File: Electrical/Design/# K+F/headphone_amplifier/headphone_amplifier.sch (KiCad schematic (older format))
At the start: 6 parts

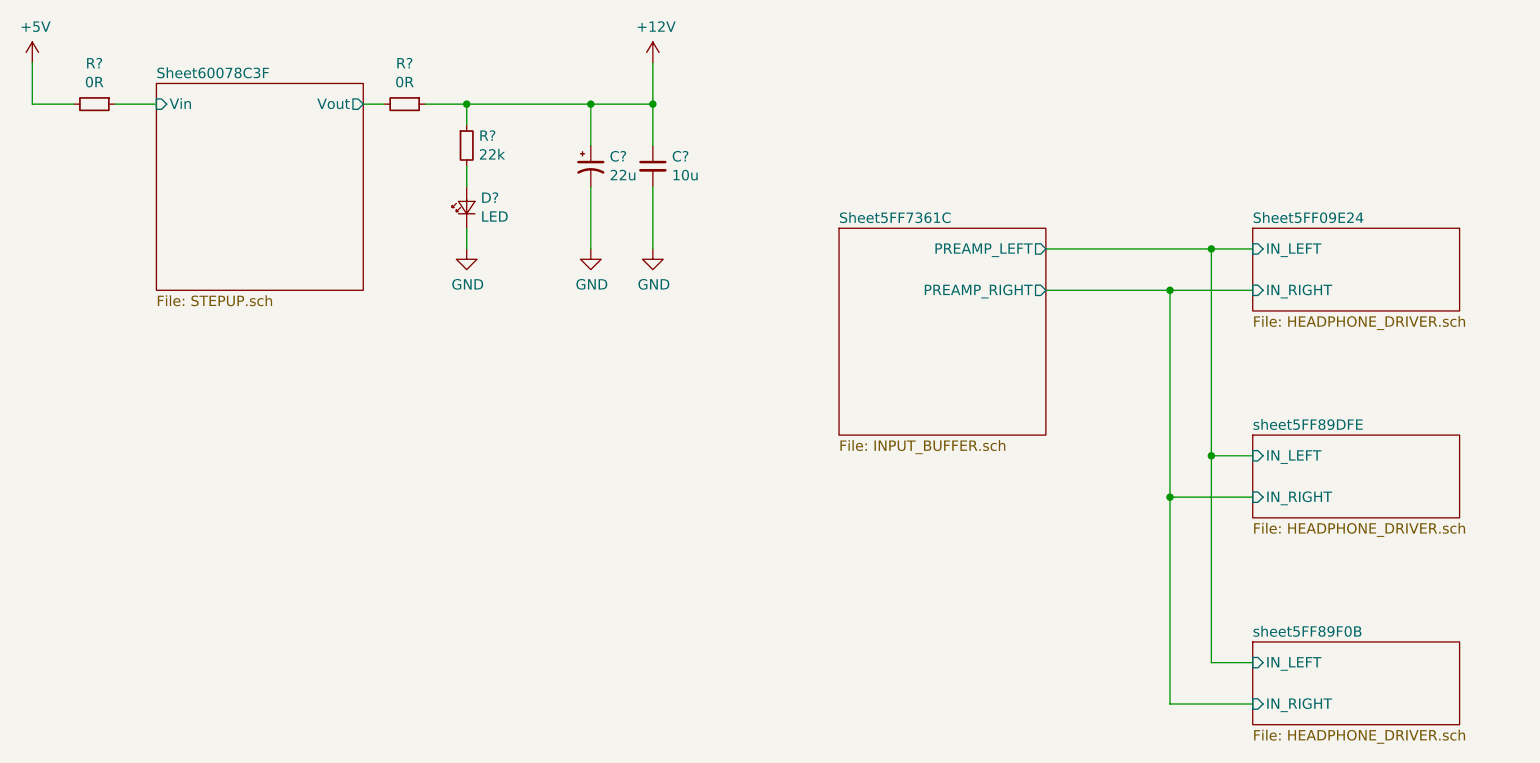
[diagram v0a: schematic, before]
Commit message: SUKU headphone_amplifier schematic fix and simulation added
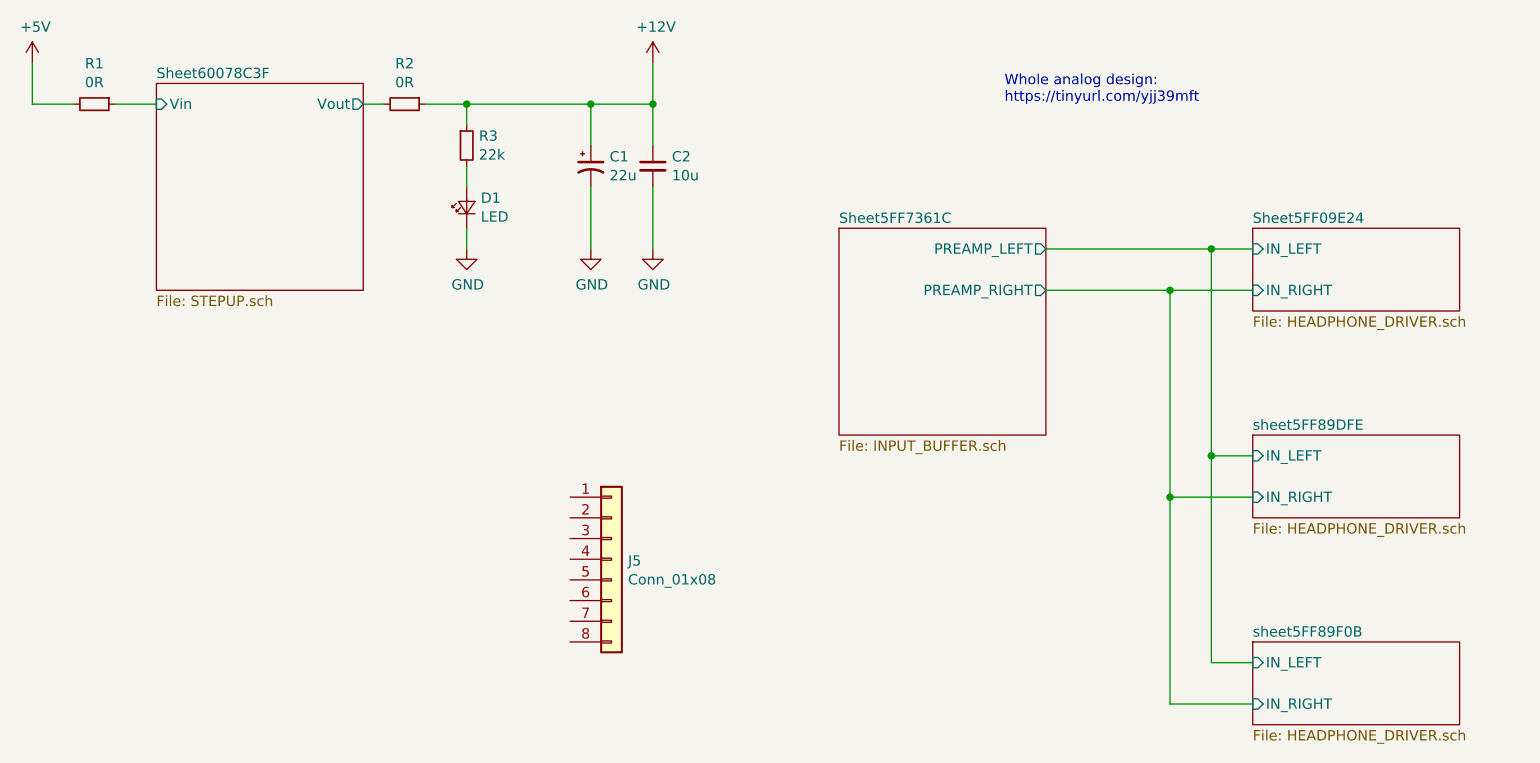
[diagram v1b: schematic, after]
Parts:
- added J5: Conn_01x08, suku_basics:grid_outline, symbol Connector_Generic:Conn_01x08
- gave numbers to parts that had none: 6
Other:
- note added: "Whole analog design:\nhttps://tinyurl.com/yjj39mft"
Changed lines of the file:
@@
 $EndDescr
 $Comp
-L suku_basics:LED D?
+L suku_basics:LED D1
 U 1 1 5FEE4BEA
 P 5700 2500
-F 0 "D?" V 5746 2432 50  0000 R CNN
+F 0 "D1" V 5746 2432 50  0000 R CNN
 F 1 "LED" V 5655 2432 50  0000 R CNN
 F 2 "suku_basics:LED_0805" V 5700 2500 50  0001 C CNN
@@
 $EndComp
 $Comp
-L power:+12V #PWR?
+L power:+12V #PWR04
 U 1 1 5FEE6012
 P 6600 1800
-F 0 "#PWR?" H 6600 1650 50  0001 C CNN
+F 0 "#PWR04" H 6600 1650 50  0001 C CNN
 F 1 "+12V" H 6615 1973 50  0000 C CNN
 F 2 "" H 6600 1800 50  0001 C CNN
@@
 $EndComp
 $Comp
-L suku_basics:RES R?
+L suku_basics:RES R3
 U 1 1 5FEE69AC
 P 5700 2200
-F 0 "R?" H 5759 2246 50  0000 L CNN
+F 0 "R3" H 5759 2246 50  0000 L CNN
 F 1 "22k" H 5759 2155 50  0000 L CNN
 F 2 "suku_basics:RES_0805" H 5700 2200 50  0001 C CNN
@@
 $EndComp
 $Comp
-L power:GND #PWR?
+L power:GND #PWR02
 U 1 1 5FEE7098
 P 5700 2700
-F 0 "#PWR?" H 5700 2450 50  0001 C CNN
+F 0 "#PWR02" H 5700 2450 50  0001 C CNN
 F 1 "GND" H 5705 2527 50  0000 C CNN
 F 2 "" H 5700 2700 50  0001 C CNN
@@
 	6600 2000 6600 1800
 $Comp
-L suku_basics:CAP C?
+L suku_basics:CAP C2
 U 1 1 5FF99EA8
 P 6600 2300
-F 0 "C?" H 6692 2346 50  0000 L CNN
+F 0 "C2" H 6692 2346 50  0000 L CNN
 F 1 "10u" H 6692 2255 50  0000 L CNN
 F 2 "suku_basics:CAP_0805" H 6600 2300 50  0001 C CNN
@@
 $EndComp
 $Comp
-L suku_basics:CAP_POL C?
+L suku_basics:CAP_POL C1
 U 1 1 5FF9BCBF
 P 6300 2300
-AR Path="/5FF9BCBF" Ref="C?"  Part="1"
+AR Path="/5FF9BCBF" Ref="C1"  Part="1"
 AR Path="/5FF7361D/5FF9BCBF" Ref="C?"  Part="1"
-F 0 "C?" H 6391 2346 50  0000 L CNN
+F 0 "C1" H 6391 2346 50  0000 L CNN
 F 1 "22u" H 6391 2255 50  0000 L CNN
 F 2 "" H 6300 2300 50  0001 C CNN
@@
 $EndComp
 $Comp
-L power:GND #PWR?
+L power:GND #PWR03
 U 1 1 5FF9CB04
 P 6300 2700
-F 0 "#PWR?" H 6300 2450 50  0001 C CNN
+F 0 "#PWR03" H 6300 2450 50  0001 C CNN
 F 1 "GND" H 6305 2527 50  0000 C CNN
 F 2 "" H 6300 2700 50  0001 C CNN
@@
 	6300 2700 6300 2400
 $Comp
-L power:GND #PWR?
+L power:GND #PWR05
 U 1 1 5FF9D16F
 P 6600 2700
-F 0 "#PWR?" H 6600 2450 50  0001 C CNN
+F 0 "#PWR05" H 6600 2450 50  0001 C CNN
 F 1 "GND" H 6605 2527 50  0000 C CNN
 F 2 "" H 6600 2700 50  0001 C CNN
@@
 Connection ~ 6600 2000
 $Comp
-L suku_basics:RES R?
+L suku_basics:RES R1
 U 1 1 60074023
 P 3900 2000
-F 0 "R?" V 3704 2000 50  0000 C CNN
+F 0 "R1" V 3704 2000 50  0000 C CNN
 F 1 "0R" V 3795 2000 50  0000 C CNN
 F 2 "suku_basics:RES_0805" H 3900 2000 50  0001 C CNN
@@
 	3800 2000 3600 2000
 $Comp
-L power:+5V #PWR?
+L power:+5V #PWR01
 U 1 1 6007402A
 P 3600 1800
-F 0 "#PWR?" H 3600 1650 50  0001 C CNN
+F 0 "#PWR01" H 3600 1650 50  0001 C CNN
 F 1 "+5V" H 3615 1973 50  0000 C CNN
 F 2 "" H 3600 1800 50  0001 C CNN
@@
 	3600 1800 3600 2000
 $Comp
-L suku_basics:RES R?
+L suku_basics:RES R2
 U 1 1 600765BD
 P 5400 2000
-F 0 "R?" V 5204 2000 50  0000 C CNN
+F 0 "R2" V 5204 2000 50  0000 C CNN
 F 1 "0R" V 5295 2000 50  0000 C CNN
 F 2 "suku_basics:RES_0805" H 5400 2000 50  0001 C CNN
@@
 Wire Wire Line
 	4000 2000 4200 2000
+Text Notes 8300 2000 0    50   ~ 0
+Whole analog design:\nhttps://tinyurl.com/yjj39mft
+$Comp
+L Connector_Generic:Conn_01x08 J5
+U 1 1 605AEAE2
+P 6400 4200
+F 0 "J5" H 6480 4192 50  0000 L CNN
+F 1 "Conn_01x08" H 6480 4101 50  0000 L CNN
+F 2 "suku_basics:grid_outline" H 6400 4200 50  0001 C CNN
+F 3 "~" H 6400 4200 50  0001 C CNN
+	1    6400 4200
+	1    0    0    -1
+$EndComp
 $EndSCHEMATC
